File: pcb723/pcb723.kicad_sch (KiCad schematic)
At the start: 71 parts, among them J1 Conn_01x02_Pin, J10 Conn_01x05_Socket, J11 Conn_01x05_Socket, J2 Conn_01x02_Pin, J3 Conn_02x07_Odd_Even, J4 Conn_02x02_Odd_Even, J5 USB_C_Receptacle_USB2.0_16P, J6 Conn_02x13_Odd_Even, J7 Conn_02x14_Odd_Even, J8 Conn_02x13_Odd_Even, J9 Conn_02x12_Odd_Even, SW1 SW_Push, U1 STM32H723ZGT6, U2 AMS1117-3.3, Y1 8MHz 20pF

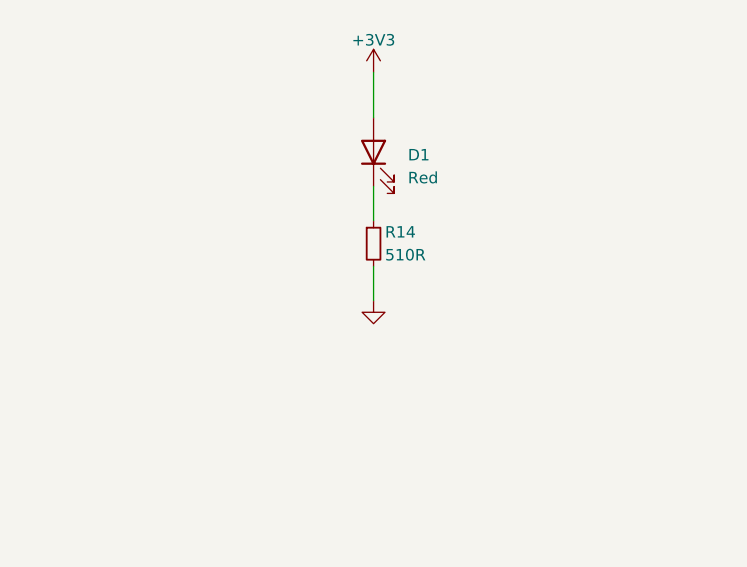
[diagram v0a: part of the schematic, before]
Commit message: R14 footprint warning fix
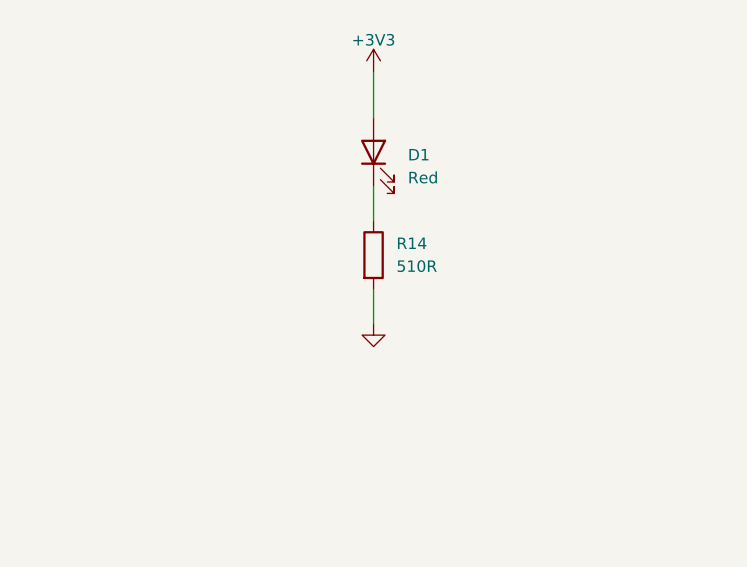
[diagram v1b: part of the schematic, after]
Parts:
- removed R14: 510R, Resistor_SMD:R_0805_2012Metric_Pad1.20x1.40mm_HandSolder, symbol Device:R_Small
- added R14: 510R, Resistor_SMD:R_0805_2012Metric_Pad1.20x1.40mm_HandSolder, symbol Device:R
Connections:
- net GND: now also R14.2
- net at D1.1 (K): now also R14.1

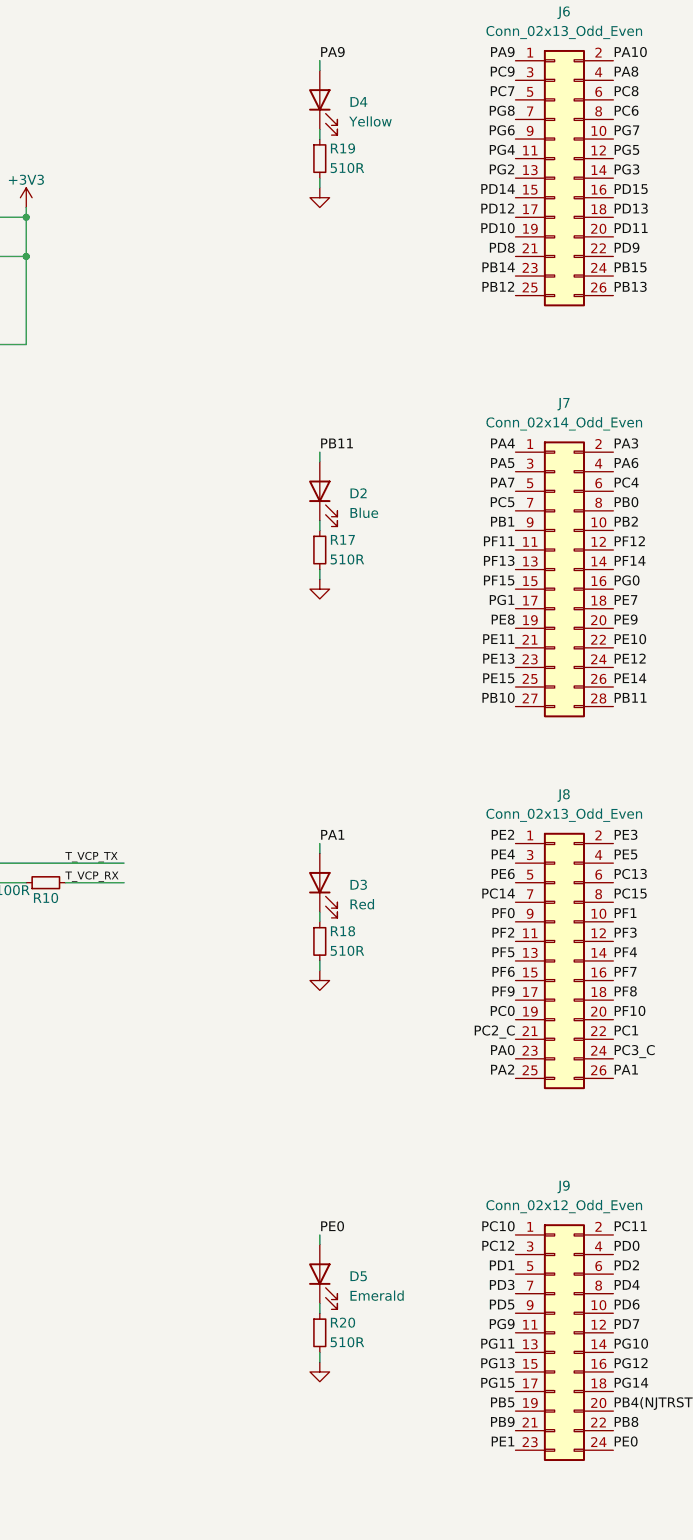
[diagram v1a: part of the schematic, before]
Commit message: User LED R footprint warning fixes
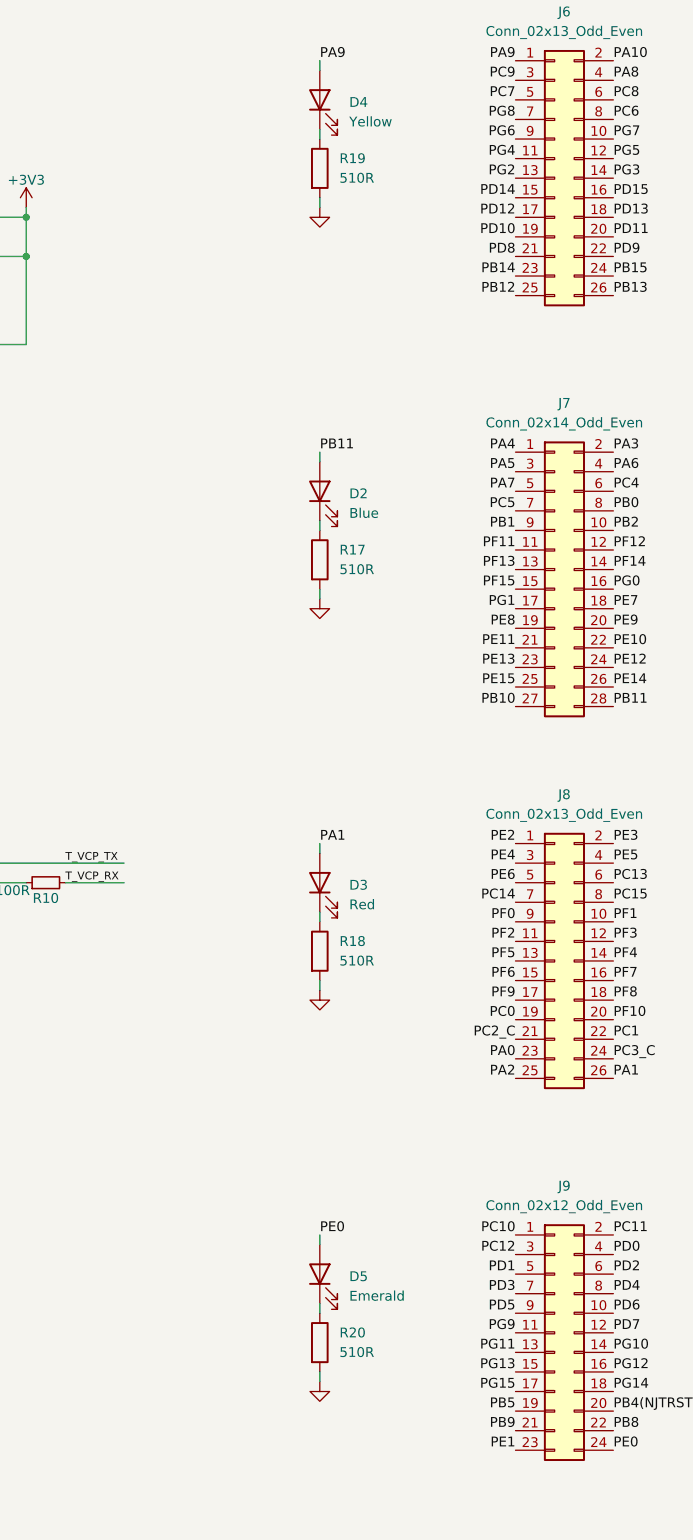
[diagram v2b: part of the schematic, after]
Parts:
- removed R17, R18, R19, R20: 510R, Resistor_SMD:R_0805_2012Metric_Pad1.20x1.40mm_HandSolder, symbol Device:R_Small
- added R17, R18, R19, R20: 510R, Resistor_SMD:R_0805_2012Metric_Pad1.20x1.40mm_HandSolder, symbol Device:R
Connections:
- net GND: now also R17.2, R18.2, R19.2, R20.2
- net at D5.1 (K): now also R20.1
- net at D3.1 (K): now also R18.1
- net at D2.1 (K): now also R17.1
- net at D4.1 (K): now also R19.1

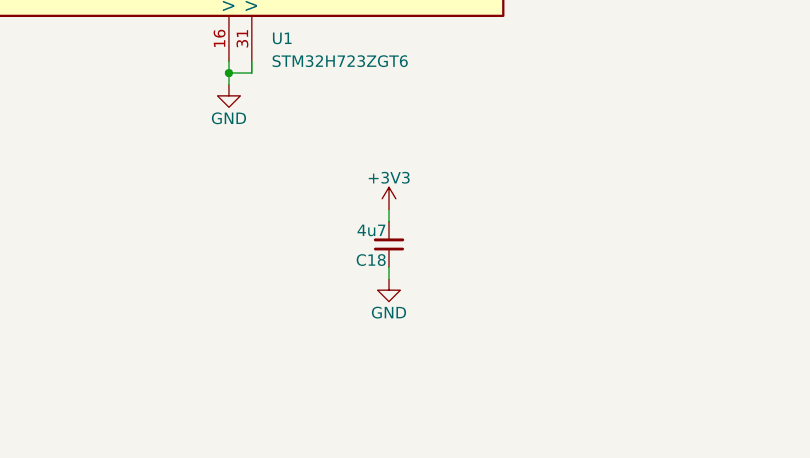
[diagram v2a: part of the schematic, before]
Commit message: Capacitor footprint warning fix
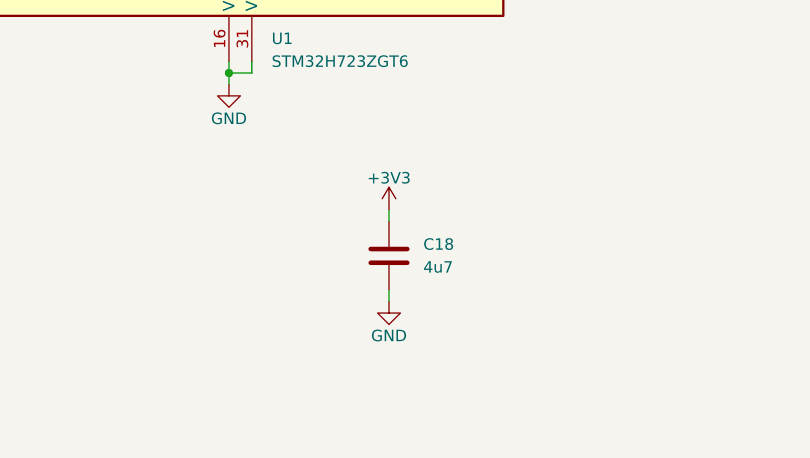
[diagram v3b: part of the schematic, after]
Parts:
- removed C18: 4u7, Capacitor_SMD:C_1206_3216Metric, symbol Device:C_Small
- added C18: 4u7, Capacitor_SMD:C_1206_3216Metric, symbol Device:C
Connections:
- net +3V3: now also C18.1
- net GND: now also C18.2

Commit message: Update footprints of capacitors
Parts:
- D2: JLC# C2293 -> (none)
- U1: JLC# C730146 -> (none)
